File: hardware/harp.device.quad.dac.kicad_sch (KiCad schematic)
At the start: 0 parts

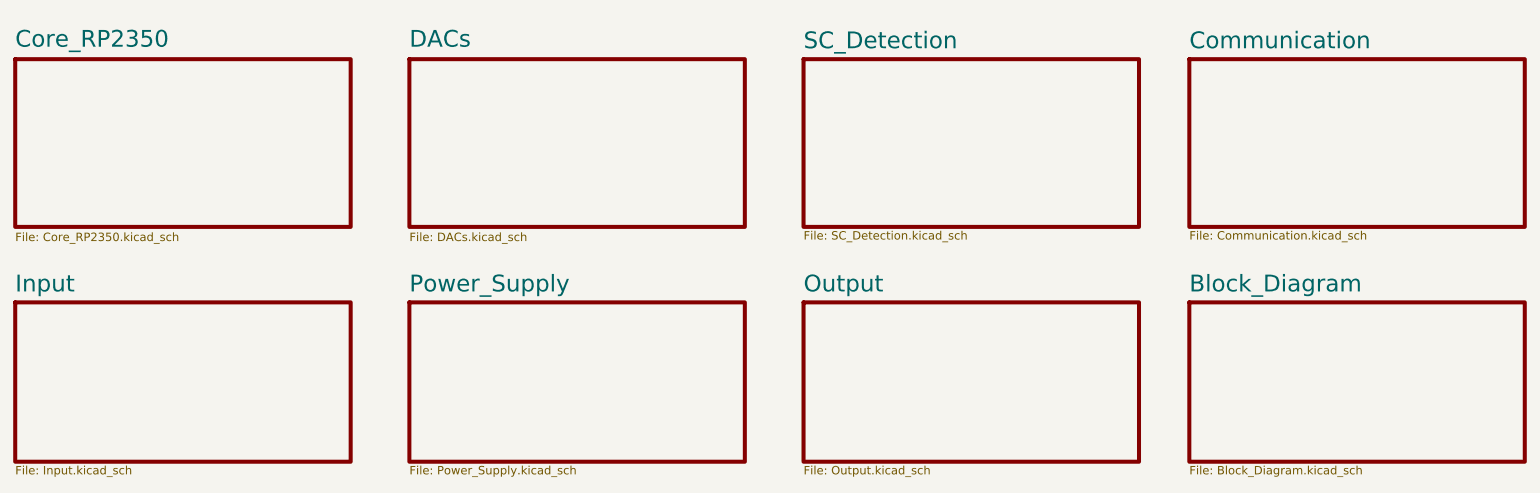
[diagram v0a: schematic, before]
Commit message: draft simplified rp2350 schematic w/sd card
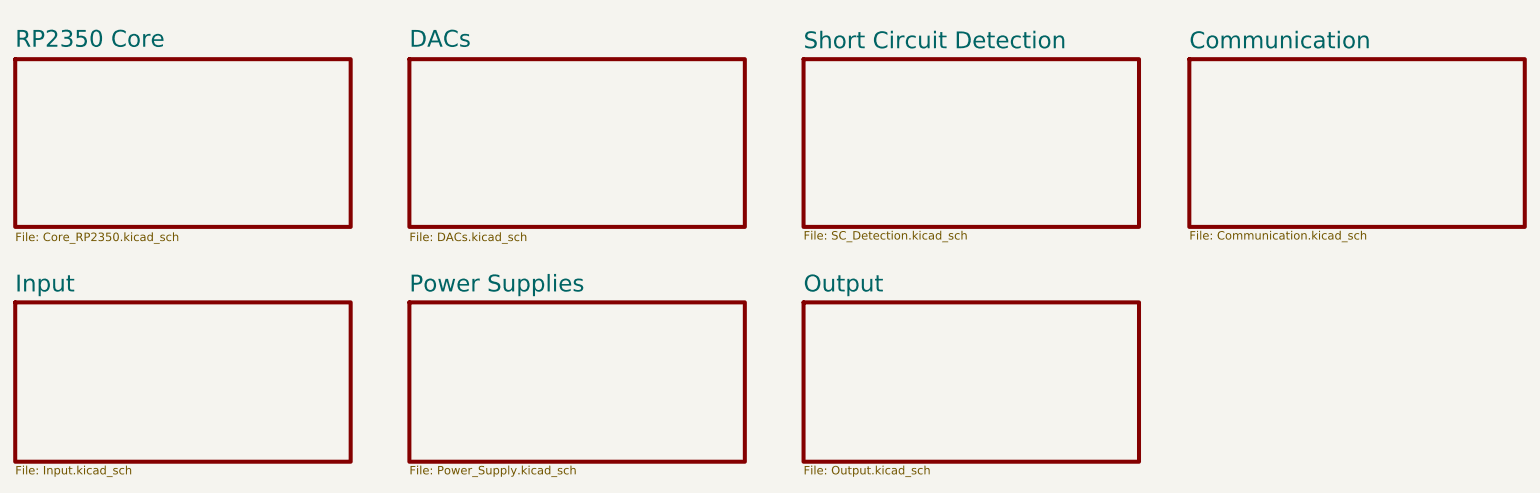
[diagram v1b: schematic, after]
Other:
- sheet Core_RP2350 renamed RP2350 Core
- sheet Power_Supply renamed Power Supplies
- sheet SC_Detection renamed Short Circuit Detection
- removed sheet Block_Diagram
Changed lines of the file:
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@@
 		(property "Sheetname" "Communication"
 			(at 210.82 29.1334 0)
-			(show_name yes)
 			(effects
 				(font
@@
 		(property "Sheetfile" "Communication.kicad_sch"
 			(at 210.82 56.4646 0)
-			(show_name yes)
 			(effects
 				(font
@@
 				(path "/6b47c519-21c4-43bd-9777-b273999e4447"
 					(page "4")
-				)
-			)
-		)
-	)
-	(sheet
-		(at 210.82 67.31)
-		(size 50.8 24.13)
-		(exclude_from_sim no)
-		(in_bom yes)
-		(on_board yes)
-		(dnp no)
-		(fields_autoplaced yes)
-		(stroke
-			(width 0.6096)
-			(type solid)
-			(color 0 0 255 1)
-		)
-		(fill
-			(color 255 255 160 1.0000)
-		)
-		(property "Sheetname" "Block_Diagram"
-			(at 210.82 65.9634 0)
-			(show_name yes)
-			(effects
-				(font
-					(size 2.54 2.54)
-				)
-				(justify left bottom)
-			)
-		)
-		(property "Sheetfile" "Block_Diagram.kicad_sch"
-			(at 210.82 92.0246 0)
-			(show_name yes)
-			(effects
-				(font
-					(size 1.27 1.27)
-				)
-				(justify left top)
-			)
-		)
-		(instances
-			(project "harp.device.quad.dac"
-				(path "/6b47c519-21c4-43bd-9777-b273999e4447"
-					(page "8")
 				)
 			)
@@
 		(property "Sheetname" "Output"
 			(at 152.4 65.9634 0)
-			(show_name yes)
 			(effects
 				(font
@@
 		(property "Sheetfile" "Output.kicad_sch"
 			(at 152.4 92.0246 0)
-			(show_name yes)
 			(effects
 				(font
@@
 			(color 255 255 160 1.0000)
 		)
-		(property "Sheetname" "SC_Detection"
+		(property "Sheetname" "Short Circuit Detection"
 			(at 152.4 29.1334 0)
-			(show_name yes)
 			(effects
 				(font
@@
 		(property "Sheetfile" "SC_Detection.kicad_sch"
 			(at 152.4 56.4646 0)
-			(show_name yes)
 			(effects
 				(font
@@
 		(property "Sheetname" "DACs"
 			(at 92.71 28.9048 0)
-			(show_name yes)
 			(effects
 				(font
@@
 		(property "Sheetfile" "DACs.kicad_sch"
 			(at 92.71 56.6932 0)
-			(show_name yes)
 			(effects
 				(font
@@
 			(color 255 255 160 1.0000)
 		)
-		(property "Sheetname" "Core_RP2350"
+		(property "Sheetname" "RP2350 Core"
 			(at 33.02 28.9048 0)
-			(show_name yes)
 			(effects
 				(font
@@
 		(property "Sheetfile" "Core_RP2350.kicad_sch"
 			(at 33.02 56.6932 0)
-			(show_name yes)
 			(effects
 				(font
@@
 		(property "Sheetname" "Input"
 			(at 33.02 65.9634 0)
-			(show_name yes)
 			(effects
 				(font
@@
 		(property "Sheetfile" "Input.kicad_sch"
 			(at 33.02 92.0246 0)
-			(show_name yes)
 			(effects
 				(font
@@
 			(color 255 255 160 1.0000)
 		)
-		(property "Sheetname" "Power_Supply"
+		(property "Sheetname" "Power Supplies"
 			(at 92.71 65.9634 0)
-			(show_name yes)
 			(effects
 				(font
@@
 		(property "Sheetfile" "Power_Supply.kicad_sch"
 			(at 92.71 92.0246 0)
-			(show_name yes)
-			(effects
-				(font
+			(effects
+				(font

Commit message: draft new analog signal chain & short-circuit detection
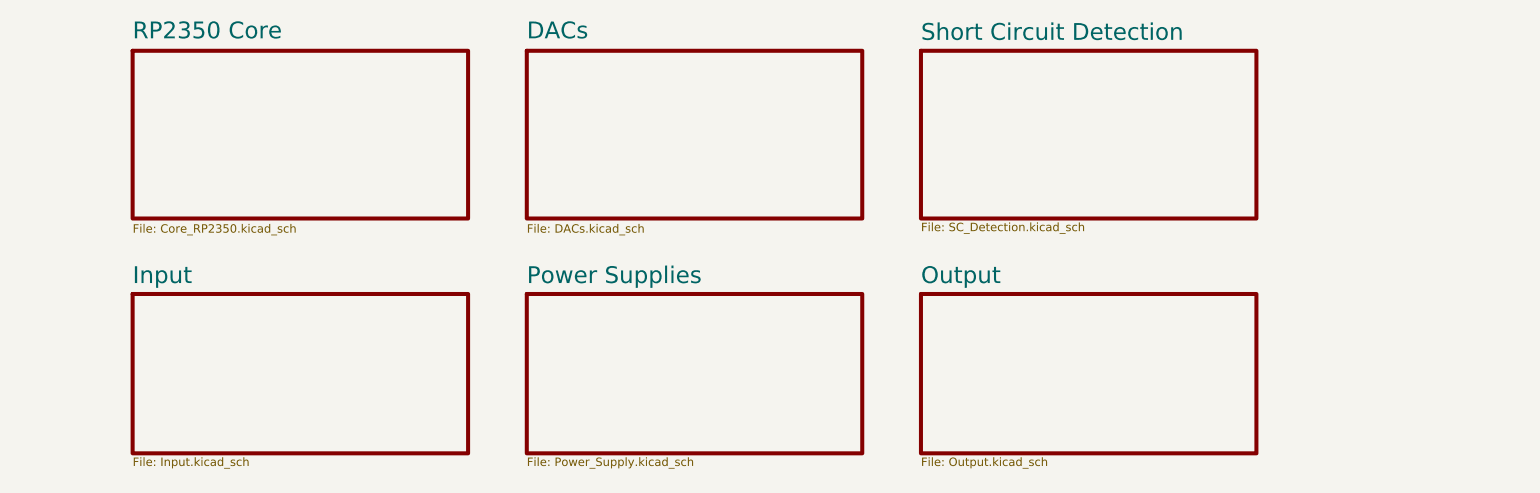
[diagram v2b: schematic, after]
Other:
- removed sheet Communication
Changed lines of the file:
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@@
 	)
 	(sheet
-		(at 210.82 30.48)
+		(at 170.18 66.04)
+		(size 50.8 24.13)
+		(exclude_from_sim no)
+		(in_bom yes)
+		(on_board yes)
+		(dnp no)
+		(fields_autoplaced yes)
+		(stroke
+			(width 0.6096)
+			(type solid)
+			(color 0 0 255 1)
+		)
+		(fill
+			(color 255 255 160 1.0000)
+		)
+		(property "Sheetname" "Output"
+			(at 170.18 64.6934 0)
+			(effects
+				(font
+					(size 2.54 2.54)
+				)
+				(justify left bottom)
+			)
+		)
+		(property "Sheetfile" "Output.kicad_sch"
+			(at 170.18 90.7546 0)
+			(effects
+				(font
+					(size 1.27 1.27)
+				)
+				(justify left top)
+			)
+		)
+		(instances
+			(project "harp.device.quad.dac"
+				(path "/6b47c519-21c4-43bd-9777-b273999e4447"
+					(page "7")
+				)
+			)
+		)
+	)
+	(sheet
+		(at 170.18 29.21)
 		(size 50.8 25.4)
 		(exclude_from_sim no)
@@
 			(color 255 255 160 1.0000)
 		)
-		(property "Sheetname" "Communication"
-			(at 210.82 29.1334 0)
-			(effects
-				(font
-					(size 2.54 2.54)
-				)
-				(justify left bottom)
-			)
-		)
-		(property "Sheetfile" "Communication.kicad_sch"
-			(at 210.82 56.4646 0)
-			(effects
-				(font
-					(size 1.27 1.27)
-				)
-				(justify left top)
-			)
-		)
-		(instances
-			(project "harp.device.quad.dac"
-				(path "/6b47c519-21c4-43bd-9777-b273999e4447"
-					(page "4")
-				)
-			)
-		)
-	)
-	(sheet
-		(at 152.4 67.31)
+		(property "Sheetname" "Short Circuit Detection"
+			(at 170.18 27.8634 0)
+			(effects
+				(font
+					(size 2.54 2.54)
+				)
+				(justify left bottom)
+			)
+		)
+		(property "Sheetfile" "SC_Detection.kicad_sch"
+			(at 170.18 55.1946 0)
+			(effects
+				(font
+					(size 1.27 1.27)
+				)
+				(justify left top)
+			)
+		)
+		(instances
+			(project "harp.device.quad.dac"
+				(path "/6b47c519-21c4-43bd-9777-b273999e4447"
+					(page "3")
+				)
+			)
+		)
+	)
+	(sheet
+		(at 110.49 29.21)
+		(size 50.8 25.4)
+		(exclude_from_sim no)
+		(in_bom yes)
+		(on_board yes)
+		(dnp no)
+		(fields_autoplaced yes)
+		(stroke
+			(width 0.6096)
+			(type solid)
+			(color 0 0 255 1)
+		)
+		(fill
+			(color 255 255 160 1.0000)
+		)
+		(property "Sheetname" "DACs"
+			(at 110.49 27.6348 0)
+			(effects
+				(font
+					(size 2.54 2.54)
+				)
+				(justify left bottom)
+			)
+		)
+		(property "Sheetfile" "DACs.kicad_sch"
+			(at 110.49 55.4232 0)
+			(effects
+				(font
+					(size 1.27 1.27)
+				)
+				(justify left top)
+			)
+		)
+		(instances
+			(project "harp.device.quad.dac"
+				(path "/6b47c519-21c4-43bd-9777-b273999e4447"
+					(page "2")
+				)
+			)
+		)
+	)
+	(sheet
+		(at 50.8 29.21)
+		(size 50.8 25.4)
+		(exclude_from_sim no)
+		(in_bom yes)
+		(on_board yes)
+		(dnp no)
+		(fields_autoplaced yes)
+		(stroke
+			(width 0.6096)
+			(type solid)
+			(color 0 0 255 1)
+		)
+		(fill
+			(color 255 255 160 1.0000)
+		)
+		(property "Sheetname" "RP2350 Core"
+			(at 50.8 27.6348 0)
+			(effects
+				(font
+					(size 2.54 2.54)
+				)
+				(justify left bottom)
+			)
+		)
+		(property "Sheetfile" "Core_RP2350.kicad_sch"
+			(at 50.8 55.4232 0)
+			(effects
+				(font
+					(size 1.27 1.27)
+				)
+				(justify left top)
+			)
+		)
+		(instances
+			(project "harp.device.quad.dac"
+				(path "/6b47c519-21c4-43bd-9777-b273999e4447"
+					(page "1")
+				)
+			)
+		)
+	)
+	(sheet
+		(at 50.8 66.04)
 		(size 50.8 24.13)
 		(exclude_from_sim no)
@@
 			(color 255 255 160 1.0000)
 		)
-		(property "Sheetname" "Output"
-			(at 152.4 65.9634 0)
-			(effects
-				(font
-					(size 2.54 2.54)
-				)
-				(justify left bottom)
-			)
-		)
-		(property "Sheetfile" "Output.kicad_sch"
-			(at 152.4 92.0246 0)
-			(effects
-				(font
-					(size 1.27 1.27)
-				)
-				(justify left top)
-			)
-		)
-		(instances
-			(project "harp.device.quad.dac"
-				(path "/6b47c519-21c4-43bd-9777-b273999e4447"
-					(page "7")
-				)
-			)
-		)
-	)
-	(sheet
-		(at 152.4 30.48)
-		(size 50.8 25.4)
-		(exclude_from_sim no)
-		(in_bom yes)
-		(on_board yes)
-		(dnp no)
-		(fields_autoplaced yes)
-		(stroke
-			(width 0.6096)
-			(type solid)
-			(color 0 0 255 1)
-		)
-		(fill
-			(color 255 255 160 1.0000)
-		)
-		(property "Sheetname" "Short Circuit Detection"
-			(at 152.4 29.1334 0)
-			(effects
-				(font
-					(size 2.54 2.54)
-				)
-				(justify left bottom)
-			)
-		)
-		(property "Sheetfile" "SC_Detection.kicad_sch"
-			(at 152.4 56.4646 0)
-			(effects
-				(font
-					(size 1.27 1.27)
-				)
-				(justify left top)
-			)
-		)
-		(instances
-			(project "harp.device.quad.dac"
-				(path "/6b47c519-21c4-43bd-9777-b273999e4447"
-					(page "3")
-				)
-			)
-		)
-	)
-	(sheet
-		(at 92.71 30.48)
-		(size 50.8 25.4)
-		(exclude_from_sim no)
-		(in_bom yes)
-		(on_board yes)
-		(dnp no)
-		(fields_autoplaced yes)
-		(stroke
-			(width 0.6096)
-			(type solid)
-			(color 0 0 255 1)
-		)
-		(fill
-			(color 255 255 160 1.0000)
-		)
-		(property "Sheetname" "DACs"
-			(at 92.71 28.9048 0)
-			(effects
-				(font
-					(size 2.54 2.54)
-				)
-				(justify left bottom)
-			)
-		)
-		(property "Sheetfile" "DACs.kicad_sch"
-			(at 92.71 56.6932 0)
-			(effects
-				(font
-					(size 1.27 1.27)
-				)
-				(justify left top)
-			)
-		)
-		(instances
-			(project "harp.device.quad.dac"
-				(path "/6b47c519-21c4-43bd-9777-b273999e4447"
-					(page "2")
-				)
-			)
-		)
-	)
-	(sheet
-		(at 33.02 30.48)
-		(size 50.8 25.4)
-		(exclude_from_sim no)
-		(in_bom yes)
-		(on_board yes)
-		(dnp no)
-		(fields_autoplaced yes)
-		(stroke
-			(width 0.6096)
-			(type solid)
-			(color 0 0 255 1)
-		)
-		(fill
-			(color 255 255 160 1.0000)
-		)
-		(property "Sheetname" "RP2350 Core"
-			(at 33.02 28.9048 0)
-			(effects
-				(font
-					(size 2.54 2.54)
-				)
-				(justify left bottom)
-			)
-		)
-		(property "Sheetfile" "Core_RP2350.kicad_sch"
-			(at 33.02 56.6932 0)
-			(effects
-				(font
-					(size 1.27 1.27)
-				)
-				(justify left top)
-			)
-		)
-		(instances
-			(project "harp.device.quad.dac"
-				(path "/6b47c519-21c4-43bd-9777-b273999e4447"
-					(page "1")
-				)
-			)
-		)
-	)
-	(sheet
-		(at 33.02 67.31)
+		(property "Sheetname" "Input"
+			(at 50.8 64.6934 0)
+			(effects
+				(font
+					(size 2.54 2.54)
+				)
+				(justify left bottom)
+			)
+		)
+		(property "Sheetfile" "Input.kicad_sch"
+			(at 50.8 90.7546 0)
+			(effects
+				(font
+					(size 1.27 1.27)
+				)
+				(justify left top)
+			)
+		)
+		(instances
+			(project "harp.device.quad.dac"
+				(path "/6b47c519-21c4-43bd-9777-b273999e4447"
+					(page "5")
+				)
+			)
+		)
+	)
+	(sheet
+		(at 110.49 66.04)
 		(size 50.8 24.13)
 		(exclude_from_sim no)
@@
 			(color 255 255 160 1.0000)
 		)
-		(property "Sheetname" "Input"
-			(at 33.02 65.9634 0)
-			(effects
-				(font
-					(size 2.54 2.54)
-				)
-				(justify left bottom)
-			)
-		)
-		(property "Sheetfile" "Input.kicad_sch"
-			(at 33.02 92.0246 0)
-			(effects
-				(font
-					(size 1.27 1.27)
-				)
-				(justify left top)
-			)
-		)
-		(instances
-			(project "harp.device.quad.dac"
-				(path "/6b47c519-21c4-43bd-9777-b273999e4447"
-					(page "5")
-				)
-			)
-		)
-	)
-	(sheet
-		(at 92.71 67.31)
-		(size 50.8 24.13)
-		(exclude_from_sim no)
-		(in_bom yes)
-		(on_board yes)
-		(dnp no)
-		(fields_autoplaced yes)
-		(stroke
-			(width 0.6096)
-			(type solid)
-			(color 0 0 255 1)
-		)
-		(fill
-			(color 255 255 160 1.0000)
-		)
 		(property "Sheetname" "Power Supplies"
-			(at 92.71 65.9634 0)
+			(at 110.49 64.6934 0)
 			(effects
 				(font
@@
 		)
 		(property "Sheetfile" "Power_Supply.kicad_sch"
-			(at 92.71 92.0246 0)
-			(effects
-				(font
+			(at 110.49 90.7546 0)
+			(effects
+				(font

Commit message: update tvs diodes, regulators, and power supply chain
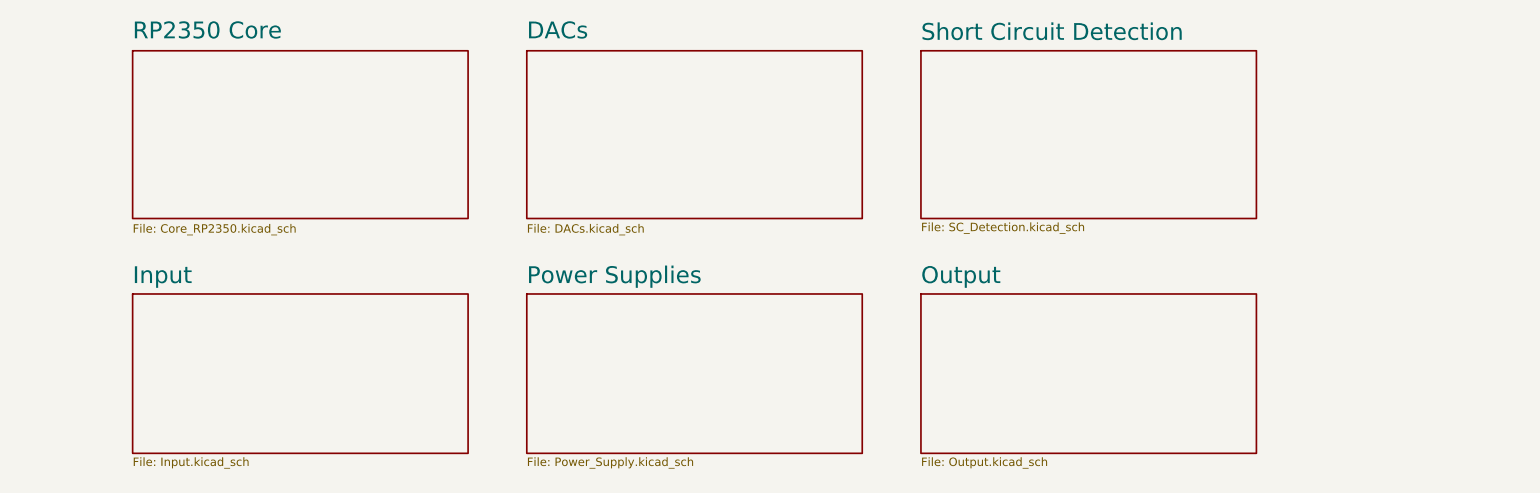
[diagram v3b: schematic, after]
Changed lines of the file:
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@@
 		(fields_autoplaced yes)
 		(stroke
-			(width 0.6096)
+			(width 0.254)
 			(type solid)
 			(color 0 0 255 1)
@@
 		(fields_autoplaced yes)
 		(stroke
-			(width 0.6096)
+			(width 0.254)
 			(type solid)
 			(color 0 0 255 1)
@@
 		(fields_autoplaced yes)
 		(stroke
-			(width 0.6096)
+			(width 0.254)
 			(type solid)
 			(color 0 0 255 1)
@@
 		(fields_autoplaced yes)
 		(stroke
-			(width 0.6096)
+			(width 0.254)
 			(type solid)
 			(color 0 0 255 1)
@@
 		(fields_autoplaced yes)
 		(stroke
-			(width 0.6096)
+			(width 0.254)
 			(type solid)
 			(color 0 0 255 1)
@@
 		(fields_autoplaced yes)
 		(stroke
-			(width 0.6096)
-			(type solid)
-			(color 0 0 255 1)
+			(width 0.254)
+			(type solid)
+			(color 0 0 255 1)
